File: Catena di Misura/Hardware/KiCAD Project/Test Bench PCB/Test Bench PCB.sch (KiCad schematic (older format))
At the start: 18 parts, among them J1 Screw_Terminal_01x02, J2 Screw_Terminal_01x02, J3 Screw_Terminal_01x02, J4 Screw_Terminal_01x04, J5 Screw_Terminal_01x02, U1 AdafruitHuzzah32Breakout, U2 Adafruit_MAX31856, U3 Adafruit_MAX31856, U4 Adafruit_MAX31856, U5 Adafruit_MAX31856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

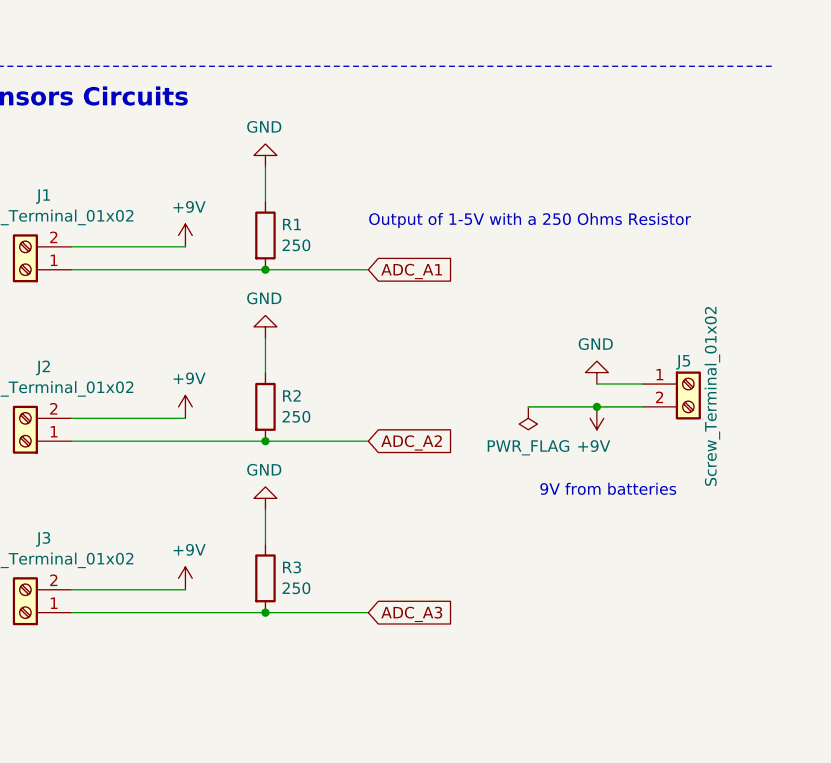
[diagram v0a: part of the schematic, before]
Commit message: Updated Component selection spreadsheet and PCB schematics
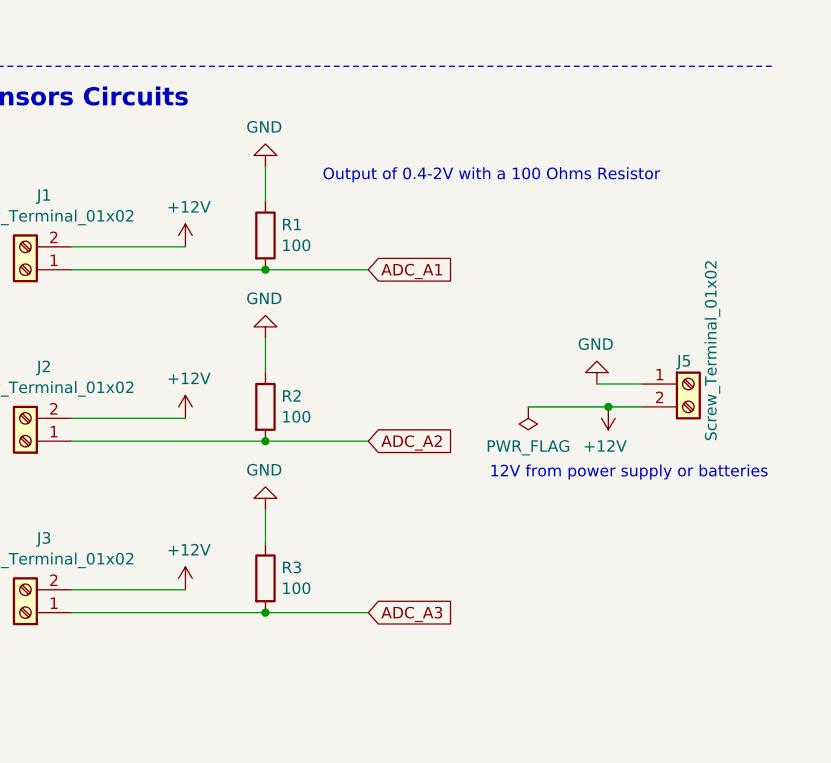
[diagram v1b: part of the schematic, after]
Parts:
- R1, R2, R3: value 250 -> 100
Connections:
- net +9V renamed +12V
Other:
- note added: "12V from power supply or batteries\n\n"
- note added: "Output of 0.4-2V with a 100 Ohms Resistor\n\n"
- note removed: "9V from batteries\n"
- note removed: "Output of 1-5V with a 250 Ohms Resistor\n\n"
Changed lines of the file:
@@
 P 9000 4550
 F 0 "R1" H 9070 4596 50  0000 L CNN
-F 1 "250" H 9070 4505 50  0000 L CNN
+F 1 "100" H 9070 4505 50  0000 L CNN
 F 2 "Resistor_THT:R_Axial_DIN0204_L3.6mm_D1.6mm_P5.08mm_Horizontal" V 8930 4550 50  0001 C CNN
 F 3 "~" H 9000 4550 50  0001 C CNN
@@
 $EndComp
 $Comp
-L power:+9V #PWR0124
-U 1 1 5F8F0040
-P 8650 4600
-F 0 "#PWR0124" H 8650 4450 50  0001 C CNN
-F 1 "+9V" H 8665 4773 50  0000 C CNN
-F 2 "" H 8650 4600 50  0001 C CNN
-F 3 "" H 8650 4600 50  0001 C CNN
-	1    8650 4600
-	1    0    0    -1
-$EndComp
-$Comp
 L power:GND #PWR0125
 U 1 1 5F8F2255
@@
 P 9000 5300
 F 0 "R2" H 9070 5346 50  0000 L CNN
-F 1 "250" H 9070 5255 50  0000 L CNN
+F 1 "100" H 9070 5255 50  0000 L CNN
 F 2 "Resistor_THT:R_Axial_DIN0204_L3.6mm_D1.6mm_P5.08mm_Horizontal" V 8930 5300 50  0001 C CNN
 F 3 "~" H 9000 5300 50  0001 C CNN
@@
 $EndComp
 $Comp
-L power:+9V #PWR0126
-U 1 1 5F8FBDCD
-P 8650 5350
-F 0 "#PWR0126" H 8650 5200 50  0001 C CNN
-F 1 "+9V" H 8665 5523 50  0000 C CNN
-F 2 "" H 8650 5350 50  0001 C CNN
-F 3 "" H 8650 5350 50  0001 C CNN
-	1    8650 5350
-	1    0    0    -1
-$EndComp
-$Comp
 L power:GND #PWR0127
 U 1 1 5F8FBDD3
@@
 P 9000 6050
 F 0 "R3" H 9070 6096 50  0000 L CNN
-F 1 "250" H 9070 6005 50  0000 L CNN
+F 1 "100" H 9070 6005 50  0000 L CNN
 F 2 "Resistor_THT:R_Axial_DIN0204_L3.6mm_D1.6mm_P5.08mm_Horizontal" V 8930 6050 50  0001 C CNN
 F 3 "~" H 9000 6050 50  0001 C CNN
@@
 $EndComp
 $Comp
-L power:+9V #PWR0128
-U 1 1 5F8FE1DF
-P 8650 6100
-F 0 "#PWR0128" H 8650 5950 50  0001 C CNN
-F 1 "+9V" H 8665 6273 50  0000 C CNN
-F 2 "" H 8650 6100 50  0001 C CNN
-F 3 "" H 8650 6100 50  0001 C CNN
-	1    8650 6100
-	1    0    0    -1
-$EndComp
-$Comp
 L power:GND #PWR0129
 U 1 1 5F8FE1E5
@@
 Wire Wire Line
 	8150 6100 8650 6100
-Text Notes 9450 4600 0    50   ~ 0
-Output of 1-5V with a 250 Ohms Resistor\n\n
+Text Notes 9250 4400 0    50   ~ 0
+Output of 0.4-2V with a 100 Ohms Resistor\n\n
 Text GLabel 2400 1300 2    50   Input ~ 0
 ADC_A1
@@
 P 10850 5200
 F 0 "J5" H 10800 5300 50  0000 L CNN
-F 1 "Screw_Terminal_01x02" V 10950 4750 50  0000 L CNN
+F 1 "Screw_Terminal_01x02" V 10950 4950 50  0000 L CNN
 F 2 "TerminalBlock:TerminalBlock_bornier-2_P5.08mm" H 10850 5200 50  0001 C CNN
 F 3 "~" H 10850 5200 50  0001 C CNN
 	1    10850 5200
 	1    0    0    -1
-$EndComp
-$Comp
-L power:+9V #PWR01
-U 1 1 5F9D30A2
-P 10450 5300
-F 0 "#PWR01" H 10450 5150 50  0001 C CNN
-F 1 "+9V" H 10465 5473 50  0000 C CNN
-F 2 "" H 10450 5300 50  0001 C CNN
-F 3 "" H 10450 5300 50  0001 C CNN
-	1    10450 5300
-	-1   0    0    1
 $EndComp
 $Comp
@@
 $EndComp
 Wire Wire Line
-	10650 5300 10450 5300
-Wire Wire Line
 	10650 5200 10450 5200
 $Comp
@@
 	-1   0    0    1
 $EndComp
-Wire Wire Line
-	10450 5300 10150 5300
-Connection ~ 10450 5300
-Text Notes 10800 5700 2    50   ~ 0
-9V from batteries\n
+Text Notes 11200 5700 2    50   ~ 0
+12V from power supply or batteries\n\n
+Wire Wire Line
+	10150 5300 10500 5300
+$Comp
+L power:+12V #PWR?
+U 1 1 5FB4126D
+P 10500 5300
+F 0 "#PWR?" H 10500 5150 50  0001 C CNN
+F 1 "+12V" H 10515 5473 50  0000 C CNN
+F 2 "" H 10500 5300 50  0001 C CNN
+F 3 "" H 10500 5300 50  0001 C CNN
+	1    10500 5300
+	-1   0    0    1
+$EndComp
+Connection ~ 10500 5300
+Wire Wire Line
+	10500 5300 10650 5300
+$Comp
+L power:+12V #PWR?
+U 1 1 5FB42063
+P 8650 6100
+F 0 "#PWR?" H 8650 5950 50  0001 C CNN
+F 1 "+12V" H 8665 6273 50  0000 C CNN
+F 2 "" H 8650 6100 50  0001 C CNN
+F 3 "" H 8650 6100 50  0001 C CNN
+	1    8650 6100
+	1    0    0    -1
+$EndComp
+$Comp
+L power:+12V #PWR?
+U 1 1 5FB428B7
+P 8650 5350
+F 0 "#PWR?" H 8650 5200 50  0001 C CNN
+F 1 "+12V" H 8665 5523 50  0000 C CNN
+F 2 "" H 8650 5350 50  0001 C CNN
+F 3 "" H 8650 5350 50  0001 C CNN
+	1    8650 5350
+	1    0    0    -1
+$EndComp
+$Comp
+L power:+12V #PWR?
+U 1 1 5FB42C6F
+P 8650 4600
+F 0 "#PWR?" H 8650 4450 50  0001 C CNN
+F 1 "+12V" H 8665 4773 50  0000 C CNN
+F 2 "" H 8650 4600 50  0001 C CNN
+F 3 "" H 8650 4600 50  0001 C CNN
+	1    8650 4600
+	1    0    0    -1
+$EndComp
 $EndSCHEMATC
